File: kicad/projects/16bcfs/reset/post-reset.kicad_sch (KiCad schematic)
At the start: 11 parts, among them SW2 SW_SPST, SW3 SW_SPST, SW4 SW_SPST, SW5 SW_SPST, U5 74HC00, U6 74HC193, U7 74HC74

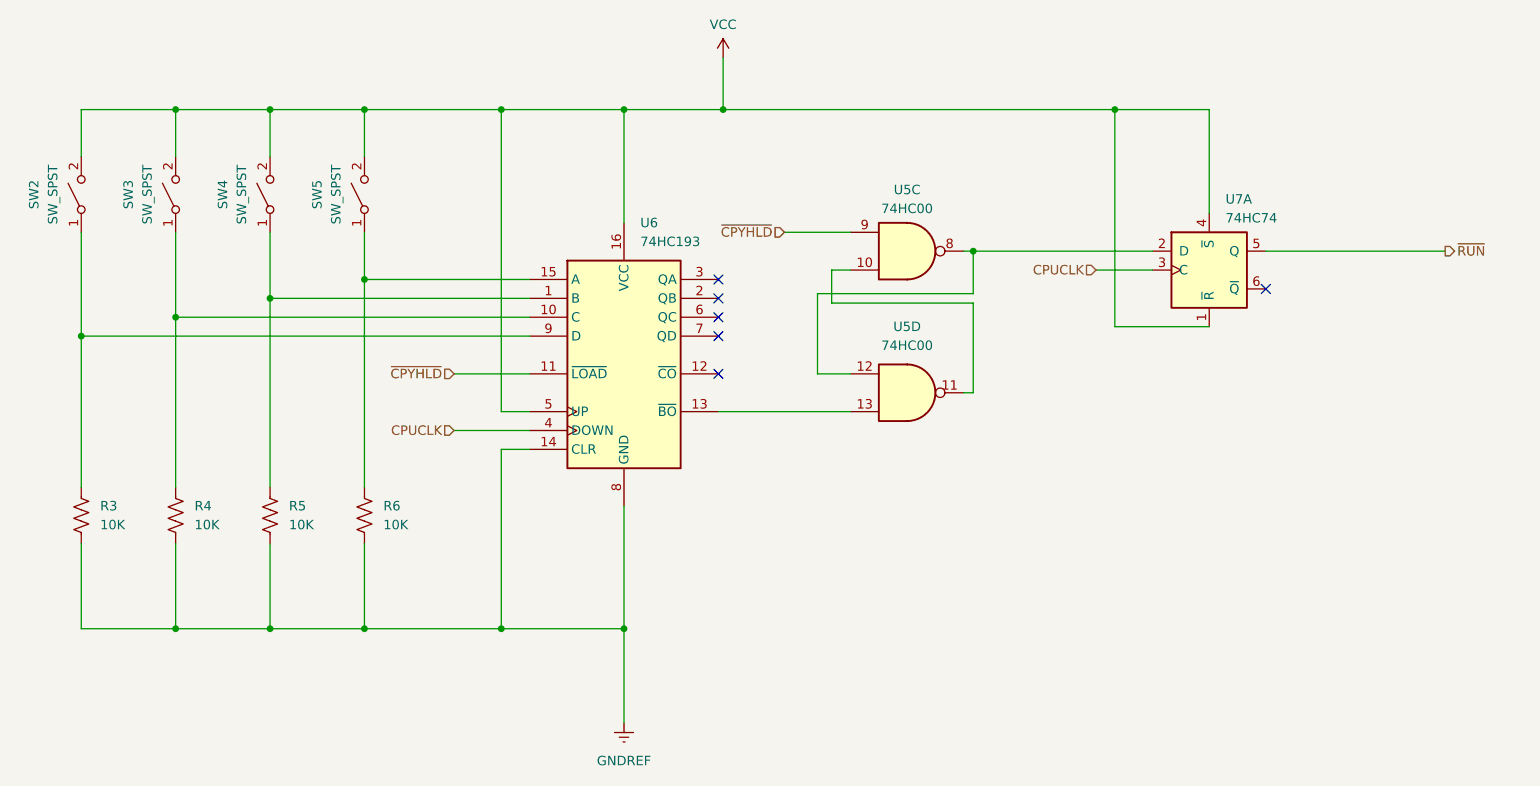
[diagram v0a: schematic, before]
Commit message: Added some debugging code
This is still not working.  I will need to revamp the reset routines for
the emulator to get this to work properly.  Everything will need an
initial state on construction and a `reset()` routine to place
everything into a proper state.  This in itself will be a major change.
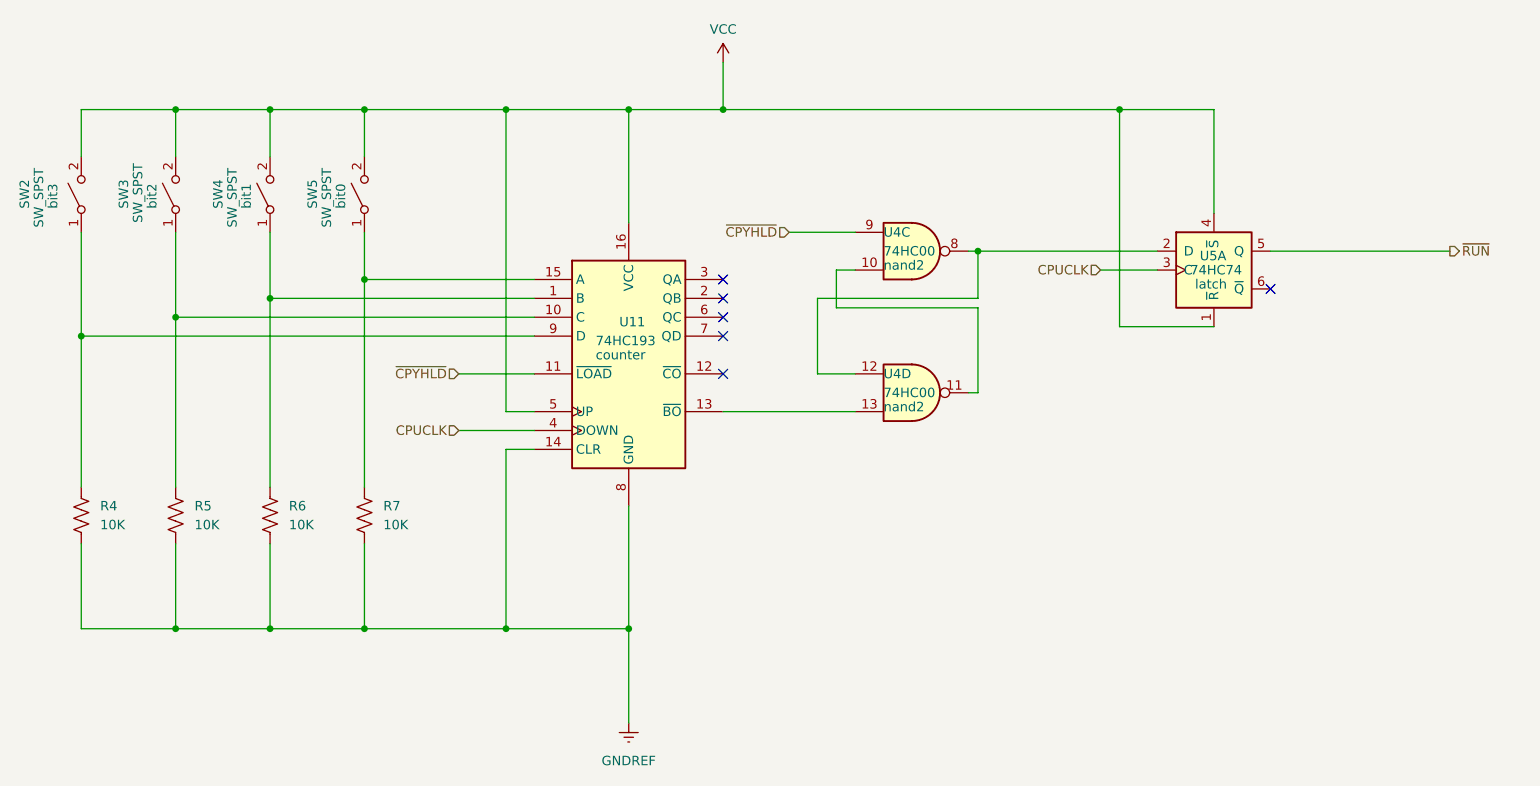
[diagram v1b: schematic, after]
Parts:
- SW2: name (none) -> bit3
- SW3: name (none) -> bit2
- SW4: name (none) -> bit1
- SW5: name (none) -> bit0
- U11: renamed from U6; name (none) -> counter
- U4: renamed from U5; name (none) -> nand2
- U5: renamed from U7; name (none) -> latch
- renumbered R3 to R4, R4 to R5, R5 to R6, R6 to R7
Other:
- moved on the sheet: U11, U4C, U4D, U5A

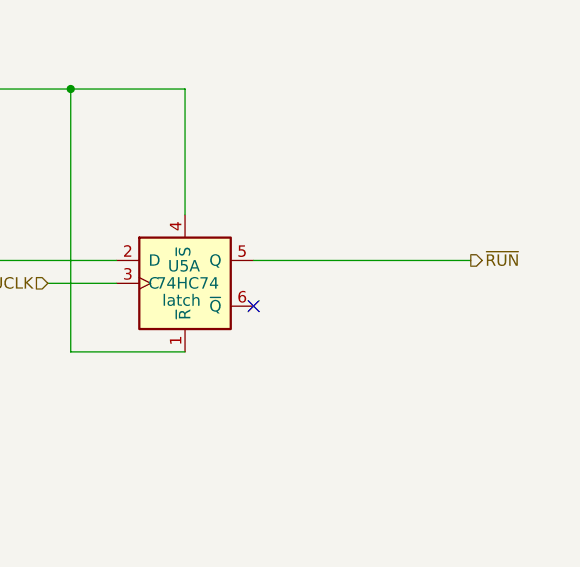
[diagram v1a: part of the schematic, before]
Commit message: Make a number of changes to the schematic and emulator
These changes are incremental to getting the emulator to work, they are
needed for making sure that the RESETTING, CLOCKING, and RUNNING signals
are processed properly.

There is also quite a bit of debugging code which gets added/removed
ahead of this commit.
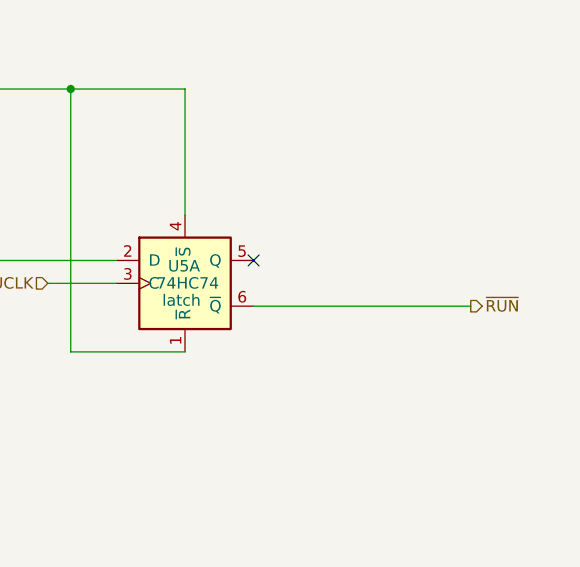
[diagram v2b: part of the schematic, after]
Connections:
- net ~{RUN}: now also U5.6 (~{Q}); no longer U5.5 (Q)
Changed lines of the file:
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@@
   (no_connect (at 138.43 95.25))
   (no_connect (at 138.43 87.63))
-  (no_connect (at 212.09 83.82))
+  (no_connect (at 212.09 78.74))
   (no_connect (at 138.43 82.55))
   (no_connect (at 138.43 85.09))
@@
     (stroke (width 0) (type default))
   )
-  (wire (pts (xy 236.22 78.74) (xy 212.09 78.74))
+  (wire (pts (xy 236.22 83.82) (xy 212.09 83.82))
     (stroke (width 0) (type default))
   )
@@
     (effects (font (size 1.27 1.27)) (justify right))
   )
-  (hierarchical_label "~{RUN}" (shape output) (at 236.22 78.74 0) (fields_autoplaced)
+  (hierarchical_label "~{RUN}" (shape output) (at 236.22 83.82 0) (fields_autoplaced)
     (effects (font (size 1.27 1.27)) (justify left))
   )
@@
     )
   )
-  (netclass_flag "" (length 2.54) (shape round) (at 212.09 78.74 0) (fields_autoplaced)
-    (effects (font (size 1.27 1.27)) (justify left bottom))
-    (property "Netclass" "latch - Q1" (at 212.7885 76.2 0)
-      (effects (font (size 1.27 1.27) italic) (justify left))
-    )
+  (netclass_flag "" (length 2.54) (shape round) (at 212.09 83.82 0) (fields_autoplaced)
+    (effects (font (size 1.27 1.27)) (justify left bottom))
+    (property "Netclass" "latch - ~{Q1}" (at 212.7885 81.28 0)
+      (effects (font (size 1.27 1.27) italic) (justify left))
+    )

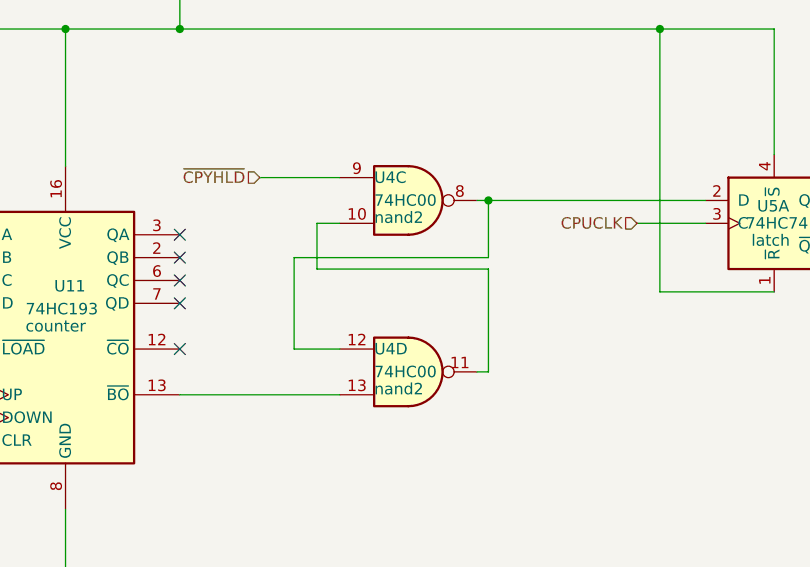
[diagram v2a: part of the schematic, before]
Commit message: Correct a save issue with KiCad
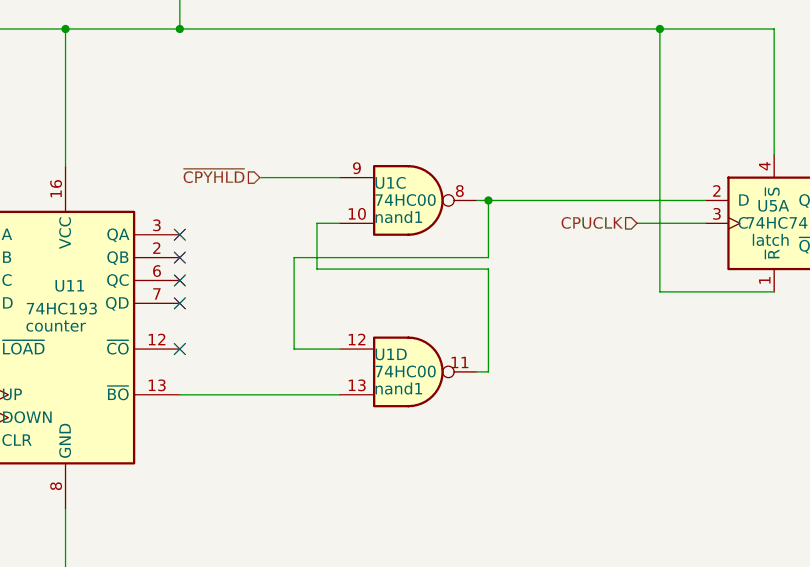
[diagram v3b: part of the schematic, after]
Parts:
- removed U4: 74HC00, symbol 74xx:74HC00
- added U1: 74HC00, symbol 74xx:74HC00
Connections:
- net ~{CPYHLD}: now also U1.9
- net at U5.2 (D): now also U1.12, U1.8
- net at U11.13 (~{BO}): now also U1.13
- new net: U1.10, U1.11
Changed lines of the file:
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@@
   (netclass_flag "" (length 2.54) (shape round) (at 171.45 78.74 0) (fields_autoplaced)
     (effects (font (size 1.27 1.27)) (justify left bottom))
-    (property "Netclass" "nand2 - Y3" (at 172.1485 76.2 0)
+    (property "Netclass" "nand1 - Y3" (at 172.1485 76.2 0)
       (effects (font (size 1.27 1.27) italic) (justify left))
     )
@@
   (netclass_flag "" (length 2.54) (shape round) (at 171.45 97.79 180) (fields_autoplaced)
     (effects (font (size 1.27 1.27)) (justify right bottom))
-    (property "Netclass" "nand2 - Y4" (at 172.1485 100.33 0)
+    (property "Netclass" "nand1 - Y4" (at 172.1485 100.33 0)
       (effects (font (size 1.27 1.27) italic) (justify left))
     )
@@
     )
   )
-  (symbol (lib_id "74xx:74HC00") (at 163.83 97.79 0) (unit 4)
-    (in_bom yes) (on_board yes) (dnp no)
-    (property "Reference" "U4" (at 160.02 95.25 0)
-      (effects (font (size 1.27 1.27)) (justify left))
-    )
-    (property "Value" "74HC00" (at 160.02 97.79 0)
-      (effects (font (size 1.27 1.27)) (justify left))
-    )
-    (property "Footprint" "" (at 163.83 97.79 0)
-      (effects (font (size 1.27 1.27)) hide)
-    )
-    (property "Datasheet" "http://www.ti.com/lit/gpn/sn74hc00" (at 163.83 97.79 0)
-      (effects (font (size 1.27 1.27)) hide)
-    )
-    (property "name" "nand2" (at 160.02 99.695 0)
-      (effects (font (size 1.27 1.27)) (justify left))
-    )
-    (pin "7")
-    (pin "10")
-    (pin "4")
-    (pin "2")
-    (pin "14")
-    (pin "1")
-    (pin "3")
-    (pin "13")
-    (pin "11")
-    (pin "6")
-    (pin "9")
-    (pin "12")
-    (pin "5")
-    (pin "8")
-    (instances
-      (project "reset"
-        (path "/d0ae44e5-d74e-4df6-bf3d-e0535c5a7785/04eaddd6-1182-4380-a007-d3b11c235b33"
-          (reference "U4") (unit 4)
-        )
-      )
-    )
-  )
   (symbol (lib_id "Device:R_US") (at 64.77 114.3 0) (unit 1)
     (in_bom yes) (on_board yes) (dnp no) (fields_autoplaced)
@@
     )
   )
-  (symbol (lib_id "74xx:74HC00") (at 163.83 78.74 0) (unit 3)
-    (in_bom yes) (on_board yes) (dnp no)
-    (property "Reference" "U4" (at 160.02 76.2 0)
-      (effects (font (size 1.27 1.27)) (justify left))
-    )
-    (property "Value" "74HC00" (at 160.02 78.74 0)
-      (effects (font (size 1.27 1.27)) (justify left))
-    )
-    (property "Footprint" "" (at 163.83 78.74 0)
-      (effects (font (size 1.27 1.27)) hide)
-    )
-    (property "Datasheet" "http://www.ti.com/lit/gpn/sn74hc00" (at 163.83 78.74 0)
-      (effects (font (size 1.27 1.27)) hide)
-    )
-    (property "name" "nand2" (at 160.02 80.645 0)
-      (effects (font (size 1.27 1.27)) (justify left))
-    )
-    (pin "7")
-    (pin "10")
-    (pin "4")
-    (pin "2")
-    (pin "14")
-    (pin "1")
-    (pin "3")
-    (pin "13")
-    (pin "11")
-    (pin "6")
-    (pin "9")
-    (pin "12")
-    (pin "5")
-    (pin "8")
-    (instances
-      (project "reset"
-        (path "/d0ae44e5-d74e-4df6-bf3d-e0535c5a7785/04eaddd6-1182-4380-a007-d3b11c235b33"
-          (reference "U4") (unit 3)
-        )
-      )
-    )
-  )
   (symbol (lib_id "Switch:SW_SPST") (at 90.17 71.12 90) (unit 1)
     (in_bom yes) (on_board yes) (dnp no)
@@
         )
       )
+    )
+  )
+  (symbol (lib_id "74xx:74HC00") (at 163.83 97.79 0) (unit 4)
+    (in_bom yes) (on_board yes) (dnp no)
+    (property "Reference" "U1" (at 160.02 95.885 0)
+      (effects (font (size 1.27 1.27)) (justify left))
+    )
+    (property "Value" "74HC00" (at 160.02 97.79 0)
+      (effects (font (size 1.27 1.27)) (justify left))
+    )
+    (property "Footprint" "" (at 163.83 97.79 0)
+      (effects (font (size 1.27 1.27)) hide)
+    )
+    (property "Datasheet" "http://www.ti.com/lit/gpn/sn74hc00" (at 163.83 97.79 0)
+      (effects (font (size 1.27 1.27)) hide)
+    )
+    (property "name" "nand1" (at 160.02 99.695 0)
+      (effects (font (size 1.27 1.27)) (justify left))
+    )
+    (pin "14")
+    (pin "7")
+    (pin "13")
+    (pin "10")
+    (pin "6")
+    (pin "12")
+    (pin "9")
+    (pin "2")
+    (pin "3")
+    (pin "1")
+    (pin "4")
+    (pin "5")
+    (pin "11")
+    (pin "8")
+    (instances
+      (project "reset"
+        (path "/d0ae44e5-d74e-4df6-bf3d-e0535c5a7785/04eaddd6-1182-4380-a007-d3b11c235b33"
+          (reference "U1") (unit 4)
+        )
+      )
+    )
+  )
+  (symbol (lib_id "74xx:74HC00") (at 163.83 78.74 0) (unit 3)
+    (in_bom yes) (on_board yes) (dnp no)
+    (property "Reference" "U1" (at 160.02 76.835 0)
+      (effects (font (size 1.27 1.27)) (justify left))
+    )
+    (property "Value" "74HC00" (at 160.02 78.74 0)
+      (effects (font (size 1.27 1.27)) (justify left))
+    )
+    (property "Footprint" "" (at 163.83 78.74 0)
+      (effects (font (size 1.27 1.27)) hide)
+    )
+    (property "Datasheet" "http://www.ti.com/lit/gpn/sn74hc00" (at 163.83 78.74 0)
+      (effects (font (size 1.27 1.27)) hide)
+    )
+    (property "name" "nand1" (at 160.02 80.645 0)
+      (effects (font (size 1.27 1.27)) (justify left))
+    )
+    (pin "14")
+    (pin "7")
+    (pin "13")
+    (pin "10")
+    (pin "6")
+    (pin "12")
+    (pin "9")
+    (pin "2")
+    (pin "3")
+    (pin "1")
+    (pin "4")
+    (pin "5")
+    (pin "11")
+    (pin "8")
+    (instances
+      (project "reset"
+        (path "/d0ae44e5-d74e-4df6-bf3d-e0535c5a7785/04eaddd6-1182-4380-a007-d3b11c235b33"
+          (reference "U1") (unit 3)
+        )
+      )
